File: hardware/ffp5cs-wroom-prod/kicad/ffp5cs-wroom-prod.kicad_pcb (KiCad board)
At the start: 2 copper layers, 150 x 100 mm, 71 parts, among them J1 Bornier_5.08, J10 JST-XH, J11 Bornier_5.08, J12 Bornier_5.08, J13 Support OLED, J14 Support I2C ext, J15 Header servo, J16 Header servo, J17 Header GPIO libres, J2 Jack 5.5/2.1, J3 Bornier_5.08, J4 Bornier_5.08, J5 Bornier_5.08, J6 Bornier_5.08, J7 JST-XH, J8 JST-XH, J9 JST-XH, K1 SRD-05VDC-SL-C, K2 SRD-05VDC-SL-C, K3 SRD-05VDC-SL-C, K4 SRD-05VDC-SL-C, Q1 BC337-40, Q2 BC337-40, Q3 BC337-40, Q4 BC337-40

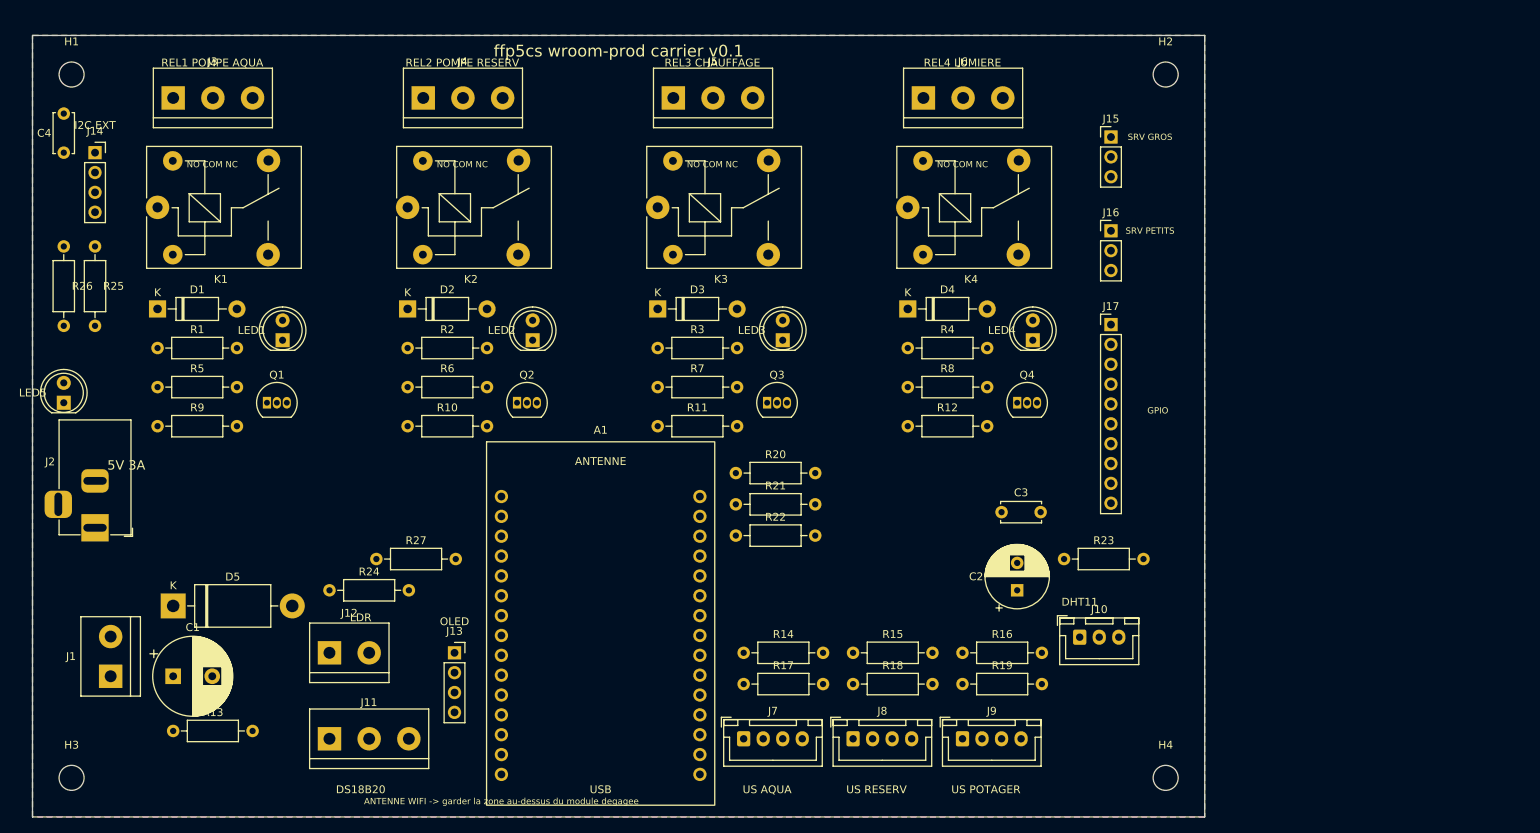
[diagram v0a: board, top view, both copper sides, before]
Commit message: hardware(ffp5cs): PCB routé + Gerbers de fabrication + câblage Fritzing
- PCB routé par freerouting 1.9 (442 segments, optimisation -52% de longueur),
  reliefs thermiques ajustés, 4 pads GND de bord en connexion pleine.
  DRC KiCad 8.0.9 : 0 violation, 0 pad non connecté.
- exports/gerbers-ffp5cs-wroom-prod-v0.2.zip : Gerbers 2 couches + masques +
  sérigraphies + Edge.Cuts + perçages Excellon PTH/NPTH (prêt JLCPCB/PCBWay).
- fritzing/ffp5cs-wroom-prod-cablage.fzz : vue breadboard du câblage
  périphériques<->DevKit (pièces core + headers génériques étiquetés),
  généré par generator/generate_fritzing.py, ouverture vérifiée dans
  Fritzing 1.0 (routing completed, aucune pièce manquante).
- README : sections routage/fabrication et Fritzing, avertissement
  « régénérer écrase le routage ».

Le checker pins.h <-> schéma <-> PCB passe toujours sur la carte routée.

Co-Authored-By: Claude Fable 5 <noreply@anthropic.com>
Claude-Session: https://claude.ai/code/session_01HcxShQb65yktRwp31wBq9q
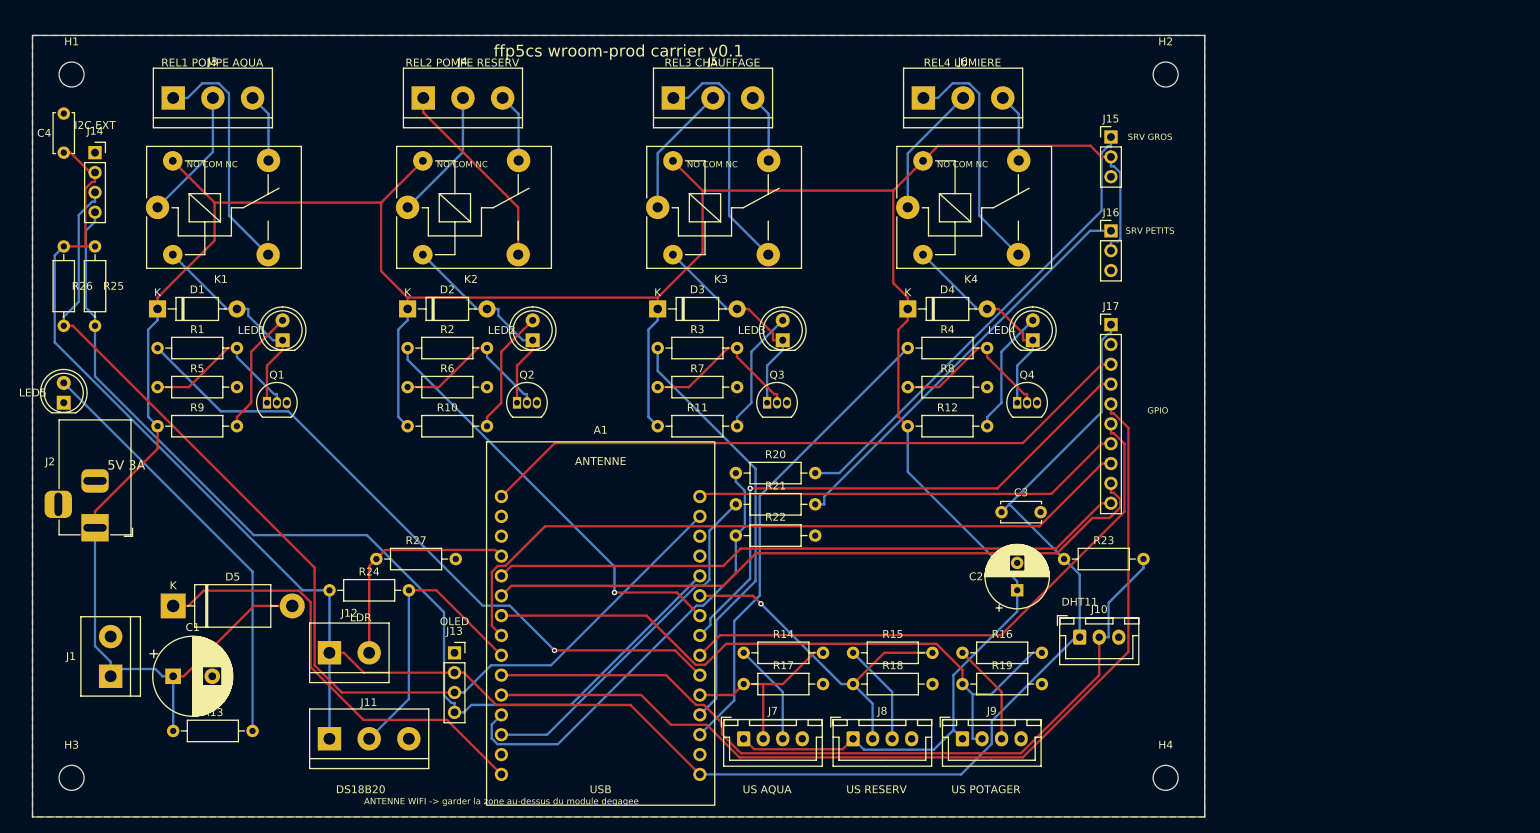
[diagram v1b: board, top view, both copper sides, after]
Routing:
- net +5V: track 0.00 -> 421.6 mm
- net +3V3: track 0.00 -> 261.7 mm
- net I2C_SCL_GPIO22: track 0.00 -> 136.4 mm
- net I2C_SDA_GPIO21: track 0.00 -> 131.4 mm
- net SPARE_GPIO14: track 0.00 -> 122.0 mm
- net DHT_GPIO27: track 0.00 -> 103.5 mm
- net SPARE_GPIO25: track 0.00 -> 93.6 mm
- net SPARE_GPIO32: track 0.00 -> 87.7 mm
- net PUMP_AQUA_GPIO16: track 0.00 -> 86.7 mm, vias 0 -> 1
- net US_POTA_GPIO33: track 0.00 -> 85.7 mm
- net EN: track 0.00 -> 85.0 mm
- net SPARE_GPIO35: track 0.00 -> 81.9 mm
- net SPARE_GPIO17: track 0.00 -> 74.1 mm
- net SPARE_GPIO5: track 0.00 -> 73.2 mm, vias 0 -> 1
- net SERVO_GROS_SIG: track 0.00 -> 60.7 mm
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
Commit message: hardware(ffp5cs): routage durci 12/24V (rev 0.3) — pistes relais 2mm, alim 1.2mm
- Classes de nets KiCad : Relais (NO/COM/NC) 2.0mm / clearance 0.5mm /
  vias 1.6mm, Alim (+5V, VIN_5V, GND) 1.2mm, signaux 0.4mm.
- Re-routage complet freerouting avec ces règles (449 segments : 28 en 2mm,
  78 en 1.2mm), zones GND reremplies.
- DRC KiCad 8.0.9 : 0 violation, 0 pad non connecté ; checker pins.h<->PCB OK.
- Sérigraphie 'SORTIES RELAIS 12/24V MAX - PAS DE 230V' près des borniers,
  title block rev 0.3.
- exports/ : gerbers v0.3 (remplacent v0.2), SVG cuivre à jour.
- README : dimensionnement courant des contacts, interdiction 230V explicitée.

Co-Authored-By: Claude Fable 5 <noreply@anthropic.com>
Claude-Session: https://claude.ai/code/session_01HcxShQb65yktRwp31wBq9q
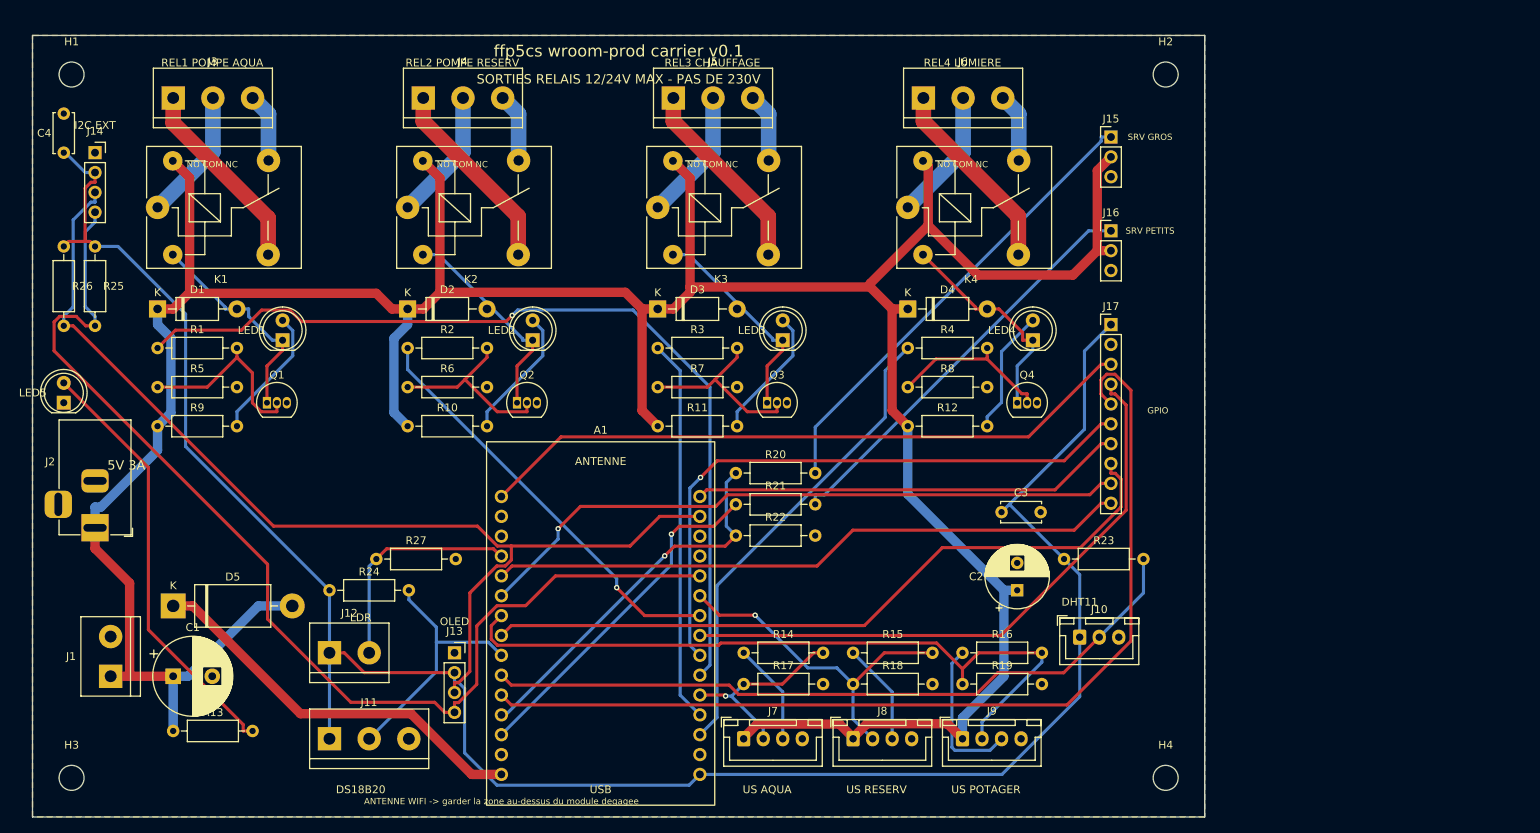
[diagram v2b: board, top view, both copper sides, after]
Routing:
- net PUMP_AQUA_GPIO16: track 86.7 -> 115.4 mm
- net I2C_SDA_GPIO21: track 131.4 -> 143.6 mm
- net DHT_GPIO27: track 103.5 -> 92.9 mm
- net SERVO_GROS_GPIO12: track 57.9 -> 48.5 mm, vias 0 -> 1
- net +5V: track 421.6 -> 430.6 mm
- net US_POTA_GPIO33: track 85.7 -> 92.8 mm
- net US_POTA_ECHO: track 13.1 -> 19.8 mm
- net VIN_5V: track 57.4 -> 50.9 mm
- net +3V3: track 261.7 -> 267.8 mm
- net REL1_NO: track 31.1 -> 25.1 mm
- net REL4_NO: track 31.1 -> 25.1 mm
- net REL3_NO: track 31.1 -> 25.1 mm
- net HEATER_GPIO2: track 55.1 -> 49.2 mm
- net SPARE_GPIO5: track 73.2 -> 78.4 mm, vias 1 -> 0
- net SPARE_GPIO17: track 74.1 -> 79.2 mm, vias 0 -> 1
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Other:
- board text added: "SORTIES RELAIS 12/24V MAX - PAS DE 230V"

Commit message: hardware(ffp5cs): 3 ports I2C libres par carte + pipeline de routage LV scripté
Demande : pouvoir brancher des modules I2C supplémentaires sans soudure.
Avec les pull-ups 4.7k en place, 3-4 modules simultanés sont confortables
(limite = capacité du bus, pas l'ESP) — dimensionné en conséquence :

- 12/24V (rev 0.4) : +J18 +J19 (supports 1x4 GND/VCC/SCL/SDA, mêmes nets
  que J14) ; netclasses Relais/Alim désormais émises par generate.py ;
  nouveau generator/route_lv.py (pipeline scripté dérivé de route_230v.py :
  freerouting, vias de couture, îlots supprimés, reliefs corrigés, bandes
  de bord) ; re-routage complet, gerbers v0.4 (remplacent v0.3).
- 230V (rev 0.2) : +J21 +J22 idem ; bandes de keepout le long des bords
  ajoutées au pipeline (l'autorouteur frôlait l'edge clearance) ;
  re-routage complet, gerbers v0.2 (remplacent v0.1).
- Validation des DEUX cartes : ERC 0 erreur, DRC 0 violation, 0 pad non
  connecté, contrôle 3mm secteur/logique (230V) : 0 écart, checker
  pins.h <-> schéma <-> PCB vert.
- READMEs : ports I2C documentés (3-4 modules max, bus < ~50cm, sinon
  pull-ups 2.2k).

Co-Authored-By: Claude Fable 5 <noreply@anthropic.com>
Claude-Session: https://claude.ai/code/session_01HcxShQb65yktRwp31wBq9q
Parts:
- added J18: Support I2C libre, ffp5cs:PinSocket_1x04_P2.54mm_Vertical, F.Cu at (171.0, 100.0)
- added J19: Support I2C libre, ffp5cs:PinSocket_1x04_P2.54mm_Vertical, F.Cu at (158.0, 100.0)
- moved C3 90.0 mm to (74.0, 106.0)
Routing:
- net GND: track 0.00 -> 484.7 mm, vias 0 -> 58
- net I2C_SCL_GPIO22: track 136.4 -> 190.9 mm, vias 0 -> 1
- net I2C_SDA_GPIO21: track 143.6 -> 196.2 mm
- net REL4_NO: track 25.1 -> 58.7 mm
- net +3V3: track 267.8 -> 301.1 mm
- net SPARE_GPIO14: track 125.1 -> 94.5 mm, vias 0 -> 1
- net PUMP_TANK_GPIO18: track 53.9 -> 84.2 mm, vias 1 -> 0
- net +5V: track 430.6 -> 457.3 mm, vias 0 -> 1
- net REL4_B: track 21.2 -> 37.9 mm
- net PUMP_AQUA_GPIO16: track 115.4 -> 103.3 mm
- net HEATER_GPIO2: track 49.2 -> 60.9 mm
- net SPARE_GPIO35: track 81.9 -> 92.7 mm
- net US_TANK_GPIO19: track 44.1 -> 54.0 mm
- net US_POTA_ECHO: track 19.8 -> 13.1 mm
- net REL3_SW: track 28.3 -> 34.0 mm
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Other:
- board text added: "I2C EXT x2"
- board text added: "ffp5cs wroom-prod carrier v0.4"
- board text removed: "SORTIES RELAIS 12/24V MAX - PAS DE 230V"
- board text removed: "ffp5cs wroom-prod carrier v0.1"

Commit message: feat(ffp5cs+hardware): relais AUX1/AUX2 (firmware v15.26, carte 230V 6 canaux) + corrections des 2 cartes
FIRMWARE ffp5cs v15.26 :
- Pins::AUX1/AUX2 (WROOM 23/25, S3 47/48), RelayController generique,
  SystemActuators::setAux/isAuxOn, IActuators::setAux (defaut no-op,
  doubles de test intacts), GPIOMap::AUX1/AUX2 dans ALL_MAPPINGS
  (parser GET + NVS + restauration boot automatiques).
- Garde test_mapping_count_is_stable 27->29 (ajout conscient).
- Tests natifs : 54 suites PASSED ; build wroom-test SUCCESS
  (wroom-prod local refuse par design les secrets placeholder).
- Contrat POST inchange ; cote serveur : n3_serveur 6.38.0 (PR jumelle).

HARDWARE 230V rev 0.3 — 6 canaux (234x110mm) :
- +REL5/REL6 (AUX1/AUX2) : relais+bornier+fentes identiques aux 4 canaux
  metier, refs dediees (R28-R33, D6/D7, LED6/LED7, Q5/Q6, J23/J24).
- J17 breakout 1x14 -> 1x12 (IO23/IO25 ne sont plus des spares).
- Pipeline : bande secteur etendue, min via 0.5, jar freerouting 2.x,
  timeout 1500s. Valide : ERC 0, DRC 0 violation 0 non-connecte,
  controle 3mm secteur/logique 0 ecart, checker 16 signaux vert.
- Gerbers v0.3, fritzing 6 commandes relais, README.

CORRECTIONS COMMUNES (12/24V rev 0.5 + 230V) :
- BOM : ligne 'A1 (supports)' (2 barrettes femelles 1x15) — le DevKit
  est enfichable, jamais soude, mais les supports n'etaient pas commandables.
- Keepout cuivre sous l'antenne WiFi du module (2 faces) + note serigraphiee
  deplacee cote antenne (elle etait sous le corps du module, cote USB).
- Checker etendu a la topologie des canaux HC-SR04 (JST 1=+5V 2=GPIO
  3=ECHO 4=GND ; 1k serie echo ; 2k pull-down) sur les deux cartes.
- 12/24V : pinmap declare AUX1/AUX2 -> spares J17 (modules relais externes) ;
  re-route complet (jar 1.9, le 2.1 depassait le timeout sur cette carte),
  DRC 0/0, gerbers v0.5.

Co-Authored-By: Claude Fable 5 <noreply@anthropic.com>
Claude-Session: https://claude.ai/code/session_01HcxShQb65yktRwp31wBq9q
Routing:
- net PUMP_TANK_GPIO18: track 84.2 -> 58.5 mm, vias 0 -> 1
- net REL4_NO: track 58.7 -> 36.5 mm
- net REL4_B: track 37.9 -> 21.1 mm
- net LIGHT_GPIO15: track 60.5 -> 76.3 mm
- net +5V: track 457.3 -> 443.5 mm, vias 1 -> 0
- net SPARE_GPIO14: track 94.5 -> 107.0 mm, vias 1 -> 0
- net +3V3: track 301.1 -> 288.9 mm
- net HEATER_GPIO2: track 60.9 -> 71.9 mm
- net SPARE_GPIO35: track 92.7 -> 81.9 mm
- net US_POTA_GPIO33: track 94.3 -> 84.8 mm
- net SPARE_GPIO17: track 77.9 -> 86.3 mm
- net SERVO_GROS_SIG: track 59.4 -> 67.7 mm
- net US_TANK_GPIO19: track 54.0 -> 61.9 mm
- net PUMP_AQUA_GPIO16: track 103.3 -> 96.0 mm
- net DHT_GPIO27: track 90.9 -> 97.6 mm
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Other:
- board text added: "ANTENNE WIFI : zone degagee (pas de cuivre dessous)"
- board text added: "ffp5cs wroom-prod carrier v0.5"
- board text removed: "ANTENNE WIFI -> garder la zone au-dessus du module degagee"
- board text removed: "ffp5cs wroom-prod carrier v0.4"

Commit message: fix(hardware): fichiers de fabrication et sérigraphie prêts pour JLCPCB
Trois défauts trouvés en préparant une commande, sur les 3 cartes :

1. Sérigraphie sous les minima fabricant : textes de 0,8 mm de haut / 0,12 mm
   de trait, alors que JLCPCB exige 1 mm / 0,15 mm — les étiquettes de câblage
   (NO COM NC, ADC A 33, ZONE 230V - DANGER...) risquaient d'être floutées ou
   supprimées par leur DFM. Tous les textes passent à >= 1 mm / 0,16 mm.
2. Repères de composants superposés aux étiquettes (34 chevauchements, dont
   l'avertissement 230 V masqué par K3/K4). Nouveau generator/tidy_silkscreen.py :
   écarte le repère (court, recasable) sans jamais bouger l'étiquette dont la
   position porte le sens. Déterministe, idempotent, avec audit final par couche.
   Titre de la carte 12/24 V déplacé (il croisait REL2/REL3).
3. Zip Gerbers de la carte commune pollué par 6 couches de documentation
   (F.Fab, *.Courtyard, User.*, Margin) et perçages PTH/NPTH fusionnés.
   Nouveau generator/export_fab.py : exactement les 7 couches utiles + PTH/NPTH
   séparés (trous M3 non métallisés) + rendus de revue sans cartouche de page.
   Aucun script d'export n'existait dans le dépôt — les exports n'étaient pas
   reproductibles, d'où la divergence entre cartes.

Ajouts : marqueur JLCJLCJLCJLC au dos des 3 cartes (emplacement du numéro de
commande imposé au fabricant, gratuit, plutôt qu'au hasard sur une étiquette),
et hardware/COMMANDE_JLCPCB.md — réglages du formulaire expliqués un par un,
choix par carte (1 oz vs 2 oz pour le 230 V, confirmation des fentes fraisées).

Cuivre inchangé : DRC 0 violation / 0 pastille non connectée sur les 3 cartes,
règle .kicad_dru 3 mm secteur toujours vérifiée sur la carte 230 V.

Co-Authored-By: Claude Opus 5 <noreply@anthropic.com>
Claude-Session: https://claude.ai/code/session_01HcxShQb65yktRwp31wBq9q
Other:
- board text added: "JLCJLCJLCJLC"
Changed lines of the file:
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@@
 		(tags "Through hole socket strip THT 1x04 2.54mm single row")
 		(property "Reference" "J14"
-			(at 0 -2.77 0)
+			(at 0 -1.77 0)
 			(layer "F.SilkS")
 			(effects
@@
 		(tags "terminal block bornier3")
 		(property "Reference" "J4"
-			(at 5.05 -4.65 0)
+			(at 5.05 -6.65 0)
 			(layer "F.SilkS")
 			(effects
@@
 		(tags "terminal block bornier2")
 		(property "Reference" "J12"
-			(at 2.54 -5.08 0)
+			(at 2.54 -6.58 0)
 			(layer "F.SilkS")
 			(effects
@@
 		(tags "Through hole socket strip THT 1x04 2.54mm single row")
 		(property "Reference" "J13"
-			(at 0 -2.77 0)
+			(at 0 -2.27 0)
 			(layer "F.SilkS")
 			(effects
@@
 		(tags "ESP32 DevKit V1")
 		(property "Reference" "A1"
-			(at 12.7 -8.5 0)
+			(at 12.7 -10.5 0)
 			(layer "F.SilkS")
 			(effects
@@
 		(tags "connector JST XH vertical")
 		(property "Reference" "J10"
-			(at 2.5 -3.55 0)
+			(at 2.5 -2.55 0)
 			(layer "F.SilkS")
 			(effects
@@
 		(tags "Resistor Axial_DIN0207 series Axial Horizontal pin pitch 10.16mm 0.25W = 1/4W length 6.3mm diameter 2.5mm")
 		(property "Reference" "R24"
-			(at 5.08 -2.37 0)
+			(at 5.08 -1.87 0)
 			(layer "F.SilkS")
 			(effects
@@
 		(tags "terminal block bornier3")
 		(property "Reference" "J3"
-			(at 5.05 -4.65 0)
+			(at 5.05 -6.65 0)
 			(layer "F.SilkS")
 			(effects
@@
 		(tags "terminal block bornier3")
 		(property "Reference" "J5"
-			(at 5.05 -4.65 0)
+			(at 5.05 -2.65 0)
 			(layer "F.SilkS")
 			(effects
@@
 		(tags "terminal block bornier3")
 		(property "Reference" "J6"
-			(at 5.05 -4.65 0)
+			(at 5.05 -6.65 0)
 			(layer "F.SilkS")
 			(effects
@@
 		(layer "Edge.Cuts")
 	)
+	(gr_text "JLCJLCJLCJLC"
+		(at 140 140.5 0)
+		(layer "B.SilkS")
+		(effects
+			(font
+				(size 1 1)
+				(thickness 0.16)
+			)
+			(justify mirror)
+		)
+	)
 	(gr_text "5V 3A"
 		(at 52 100 0)
@@
 			(font
 				(size 1.2 1.2)
-				(thickness 0.18)
+				(thickness 0.19)
 			)
 		)
@@
 			(font
 				(size 1 1)
-				(thickness 0.15)
+				(thickness 0.16)
 			)
 		)
@@
 		(effects
 			(font
-				(size 0.8 0.8)
-				(thickness 0.12)
+				(size 1 1)
+				(thickness 0.16)
 			)
 		)
@@
 		(effects
 			(font
-				(size 0.8 0.8)
-				(thickness 0.12)
+				(size 1 1)
+				(thickness 0.16)
 			)
 		)
@@
 		(effects
 			(font
-				(size 0.8 0.8)
-				(thickness 0.12)
+				(size 1 1)
+				(thickness 0.16)
 			)
 		)
@@
 			(font
 				(size 1 1)
-				(thickness 0.15)
+				(thickness 0.16)
 			)
 		)
@@
 		(effects
 			(font
-				(size 0.8 0.8)
-				(thickness 0.12)
+				(size 1 1)
+				(thickness 0.16)
 			)
 		)
@@
 		(effects
 			(font
-				(size 0.8 0.8)
-				(thickness 0.12)
+				(size 1 1)
+				(thickness 0.16)
 			)
 		)
@@
 			(font
 				(size 1 1)
-				(thickness 0.15)
+				(thickness 0.16)
 			)
 		)
@@
 			(font
 				(size 1 1)
-				(thickness 0.15)
+				(thickness 0.16)
 			)
 		)
@@
 		(effects
 			(font
-				(size 0.8 0.8)
-				(thickness 0.12)
+				(size 1 1)
+				(thickness 0.16)
 			)
 		)
@@
 		(effects
 			(font
-				(size 0.8 0.8)
-				(thickness 0.12)
+				(size 1 1)
+				(thickness 0.16)
 			)
 		)
@@
 			(font
 				(size 1 1)
-				(thickness 0.15)
+				(thickness 0.16)
 			)
 		)
 	)
 	(gr_text "ffp5cs wroom-prod carrier v0.5"
-		(at 115 47 0)
+		(at 115 56 0)
 		(layer "F.SilkS")
 		(effects
 			(font
 				(size 1.5 1.5)
-				(thickness 0.22)
+				(thickness 0.24)
 			)
 		)
@@
 			(font
 				(size 1 1)
-				(thickness 0.15)
+				(thickness 0.16)
 			)
 		)
@@
 			(font
 				(size 1 1)
-				(thickness 0.15)
+				(thickness 0.16)
 			)
 		)
@@
 			(font
 				(size 1 1)
-				(thickness 0.15)
+				(thickness 0.16)
 			)
 		)
@@
 		(effects
 			(font
-				(size 0.8 0.8)
-				(thickness 0.12)
+				(size 1 1)
+				(thickness 0.16)
 			)
 		)
@@
 			(font
 				(size 1 1)
-				(thickness 0.15)
+				(thickness 0.16)
 			)
 		)
@@
 			(font
 				(size 1 1)
-				(thickness 0.15)
+				(thickness 0.16)
 			)
 		)
@@
 			(font
 				(size 1 1)
-				(thickness 0.15)
+				(thickness 0.16)
 			)
 		)
@@
 			(font
 				(size 1 1)
-				(thickness 0.15)
+				(thickness 0.16)
 			)
 		)
@@
 			(font
 				(size 1 1)
-				(thickness 0.15)
+				(thickness 0.16)
 			)
 		)
